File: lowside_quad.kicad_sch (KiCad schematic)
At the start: 18 parts, among them U30 RED, U31 RED, U32 RED, U33 RED, U39 1N4148WS, U40 1N4148WS, U45 1N4148WS, U46 1N4148WS, U47 VND7NV04TR-E, U48 VND7NV04TR-E, U49 VND7NV04TR-E, U50 VND7NV04TR-E

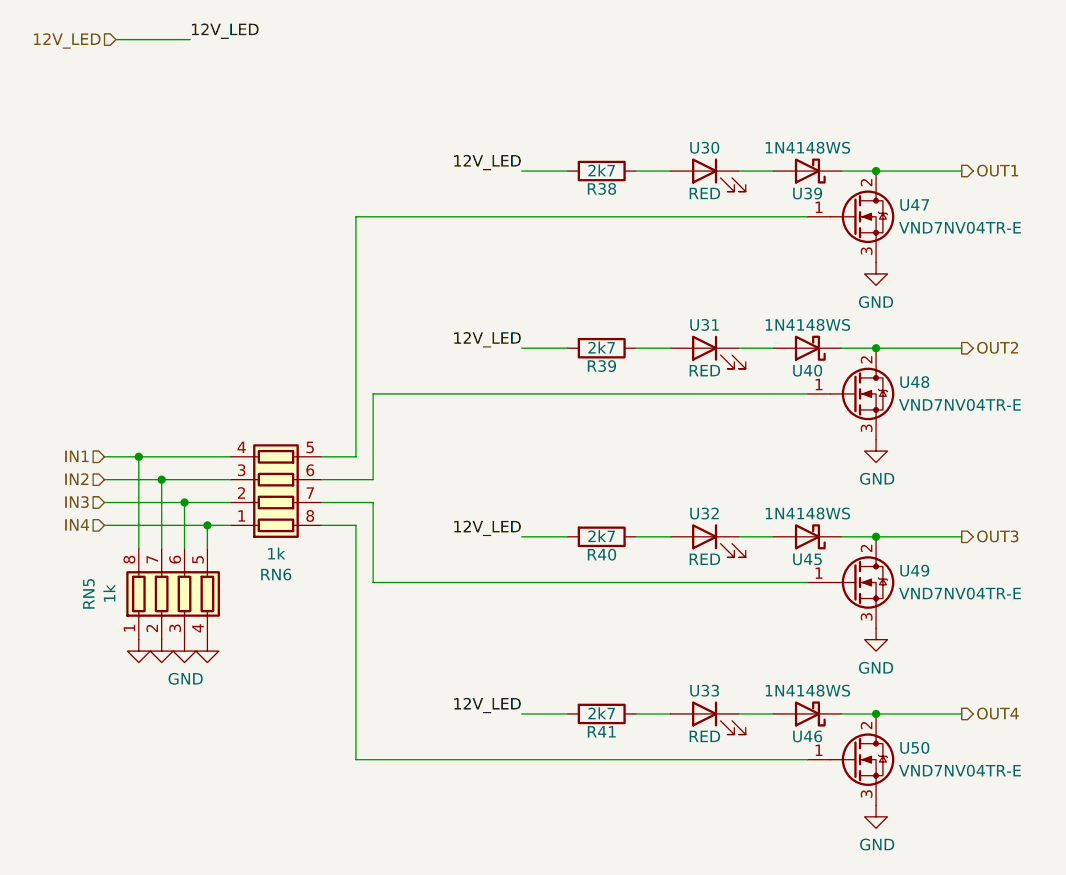
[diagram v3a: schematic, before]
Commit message: Production optimizations, voltage superv, etb sv conn
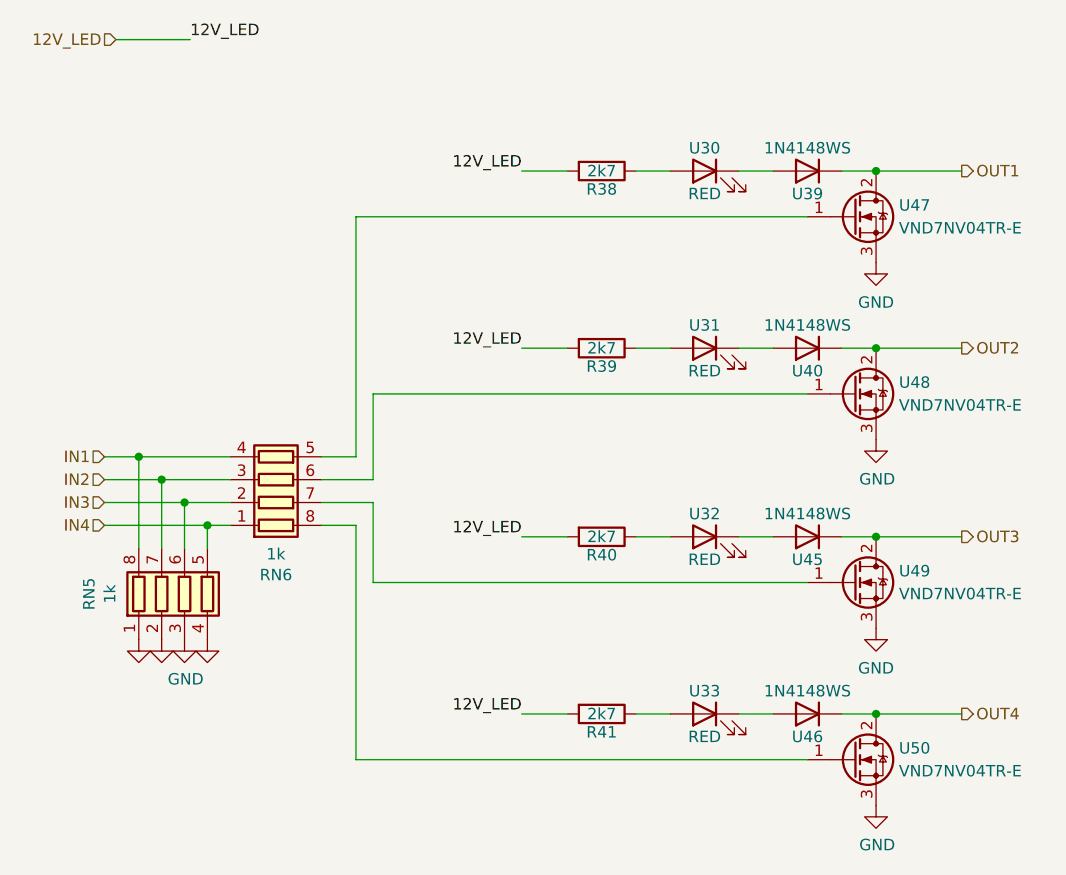
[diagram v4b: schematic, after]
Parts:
- U39, U40, U45, U46: symbol Device:D_Schottky -> Device:D
- U47, U48, U49, U50: footprint Package_TO_SOT_SMD:TO-252-2 -> Package_TO_SOT_SMD:TO-252-3_TabPin2; JLCPosOffset (none) -> 2,0; JLCRotOffset (none) -> 180; LCSC C155605 -> C262999; LCSC_alt (none) -> C155605
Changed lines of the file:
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@@
       (effects (font (size 1.27 1.27)) (justify left))
     )
-    (property "Footprint" "Package_TO_SOT_SMD:TO-252-2" (at 147.32 99.695 0)
+    (property "Footprint" "Package_TO_SOT_SMD:TO-252-3_TabPin2" (at 147.32 99.695 0)
       (effects (font (size 1.27 1.27)) hide)
     )
@@
       (effects (font (size 1.27 1.27)) hide)
     )
-    (property "LCSC" "C155605" (at 142.24 102.235 0)
+    (property "LCSC" "C262999" (at 142.24 102.235 0)
+      (effects (font (size 1.27 1.27)) hide)
+    )
+    (property "JLCPosOffset" "2,0" (at 142.24 102.235 0)
+      (effects (font (size 1.27 1.27)) hide)
+    )
+    (property "LCSC_alt" "C155605" (at 142.24 102.235 0)
+      (effects (font (size 1.27 1.27)) hide)
+    )
+    (property "JLCRotOffset" "180" (at 142.24 102.235 0)
       (effects (font (size 1.27 1.27)) hide)
     )
@@
     )
   )
-  (symbol (lib_id "Device:D_Schottky") (at 137.16 36.83 180) (unit 1)
+  (symbol (lib_id "Device:D") (at 137.16 36.83 180) (unit 1)
     (in_bom yes) (on_board yes) (dnp no)
     (property "Reference" "U39" (at 137.16 39.37 0)
@@
       (effects (font (size 1.27 1.27)) hide)
     )
-    (property "Datasheet" "" (at 137.16 36.83 0)
-      (effects (font (size 1.27 1.27)))
+    (property "Datasheet" "~" (at 137.16 36.83 0)
+      (effects (font (size 1.27 1.27)) hide)
     )
     (property "LCSC" "C2128" (at 137.16 36.83 0)
       (effects (font (size 1.27 1.27)) hide)
     )
+    (property "Sim.Device" "D" (at 137.16 36.83 0)
+      (effects (font (size 1.27 1.27)) hide)
+    )
+    (property "Sim.Pins" "1=K 2=A" (at 137.16 36.83 0)
+      (effects (font (size 1.27 1.27)) hide)
+    )
     (pin "1")
     (pin "2")
@@
       (effects (font (size 1.27 1.27)) (justify left))
     )
-    (property "Footprint" "Package_TO_SOT_SMD:TO-252-2" (at 147.32 39.37 0)
+    (property "Footprint" "Package_TO_SOT_SMD:TO-252-3_TabPin2" (at 147.32 39.37 0)
       (effects (font (size 1.27 1.27)) hide)
     )
@@
       (effects (font (size 1.27 1.27)) hide)
     )
-    (property "LCSC" "C155605" (at 142.24 41.91 0)
+    (property "LCSC" "C262999" (at 142.24 41.91 0)
+      (effects (font (size 1.27 1.27)) hide)
+    )
+    (property "JLCPosOffset" "2,0" (at 142.24 41.91 0)
+      (effects (font (size 1.27 1.27)) hide)
+    )
+    (property "LCSC_alt" "C155605" (at 142.24 41.91 0)
+      (effects (font (size 1.27 1.27)) hide)
+    )
+    (property "JLCRotOffset" "180" (at 142.24 41.91 0)
       (effects (font (size 1.27 1.27)) hide)
     )
@@
     )
   )
-  (symbol (lib_id "Device:D_Schottky") (at 137.16 97.155 180) (unit 1)
+  (symbol (lib_id "Device:D") (at 137.16 97.155 180) (unit 1)
     (in_bom yes) (on_board yes) (dnp no)
     (property "Reference" "U46" (at 137.16 99.695 0)
@@
       (effects (font (size 1.27 1.27)) hide)
     )
-    (property "Datasheet" "" (at 137.16 97.155 0)
-      (effects (font (size 1.27 1.27)))
+    (property "Datasheet" "~" (at 137.16 97.155 0)
+      (effects (font (size 1.27 1.27)) hide)
     )
     (property "LCSC" "C2128" (at 137.16 97.155 0)
       (effects (font (size 1.27 1.27)) hide)
     )
+    (property "Sim.Device" "D" (at 137.16 97.155 0)
+      (effects (font (size 1.27 1.27)) hide)
+    )
+    (property "Sim.Pins" "1=K 2=A" (at 137.16 97.155 0)
+      (effects (font (size 1.27 1.27)) hide)
+    )
     (pin "1")
     (pin "2")
@@
       (effects (font (size 1.27 1.27)) (justify left))
     )
-    (property "Footprint" "Package_TO_SOT_SMD:TO-252-2" (at 147.32 80.01 0)
+    (property "Footprint" "Package_TO_SOT_SMD:TO-252-3_TabPin2" (at 147.32 80.01 0)
       (effects (font (size 1.27 1.27)) hide)
     )
@@
       (effects (font (size 1.27 1.27)) hide)
     )
-    (property "LCSC" "C155605" (at 142.24 82.55 0)
+    (property "LCSC" "C262999" (at 142.24 82.55 0)
+      (effects (font (size 1.27 1.27)) hide)
+    )
+    (property "JLCPosOffset" "2,0" (at 142.24 82.55 0)
+      (effects (font (size 1.27 1.27)) hide)
+    )
+    (property "LCSC_alt" "C155605" (at 142.24 82.55 0)
+      (effects (font (size 1.27 1.27)) hide)
+    )
+    (property "JLCRotOffset" "180" (at 142.24 82.55 0)
       (effects (font (size 1.27 1.27)) hide)
     )
@@
     )
   )
-  (symbol (lib_id "Device:D_Schottky") (at 137.16 56.515 180) (unit 1)
+  (symbol (lib_id "Device:D") (at 137.16 56.515 180) (unit 1)
     (in_bom yes) (on_board yes) (dnp no)
     (property "Reference" "U40" (at 137.16 59.055 0)
@@
       (effects (font (size 1.27 1.27)) hide)
     )
-    (property "Datasheet" "" (at 137.16 56.515 0)
-      (effects (font (size 1.27 1.27)))
+    (property "Datasheet" "~" (at 137.16 56.515 0)
+      (effects (font (size 1.27 1.27)) hide)
     )
     (property "LCSC" "C2128" (at 137.16 56.515 0)
       (effects (font (size 1.27 1.27)) hide)
     )
+    (property "Sim.Device" "D" (at 137.16 56.515 0)
+      (effects (font (size 1.27 1.27)) hide)
+    )
+    (property "Sim.Pins" "1=K 2=A" (at 137.16 56.515 0)
+      (effects (font (size 1.27 1.27)) hide)
+    )
     (pin "1")
     (pin "2")
@@
       (effects (font (size 1.27 1.27)) (justify left))
     )
-    (property "Footprint" "Package_TO_SOT_SMD:TO-252-2" (at 147.32 59.055 0)
+    (property "Footprint" "Package_TO_SOT_SMD:TO-252-3_TabPin2" (at 147.32 59.055 0)
       (effects (font (size 1.27 1.27)) hide)
     )
@@
       (effects (font (size 1.27 1.27)) hide)
     )
-    (property "LCSC" "C155605" (at 142.24 61.595 0)
+    (property "LCSC" "C262999" (at 142.24 61.595 0)
+      (effects (font (size 1.27 1.27)) hide)
+    )
+    (property "JLCPosOffset" "2,0" (at 142.24 61.595 0)
+      (effects (font (size 1.27 1.27)) hide)
+    )
+    (property "LCSC_alt" "C155605" (at 142.24 61.595 0)
+      (effects (font (size 1.27 1.27)) hide)
+    )
+    (property "JLCRotOffset" "180" (at 142.24 61.595 0)
       (effects (font (size 1.27 1.27)) hide)
     )
@@
     )
   )
-  (symbol (lib_id "Device:D_Schottky") (at 137.16 77.47 180) (unit 1)
+  (symbol (lib_id "Device:D") (at 137.16 77.47 180) (unit 1)
     (in_bom yes) (on_board yes) (dnp no)
     (property "Reference" "U45" (at 137.16 80.01 0)
@@
       (effects (font (size 1.27 1.27)) hide)
     )
-    (property "Datasheet" "" (at 137.16 77.47 0)
-      (effects (font (size 1.27 1.27)))
+    (property "Datasheet" "~" (at 137.16 77.47 0)
+      (effects (font (size 1.27 1.27)) hide)
     )
     (property "LCSC" "C2128" (at 137.16 77.47 0)
       (effects (font (size 1.27 1.27)) hide)
     )
+    (property "Sim.Device" "D" (at 137.16 77.47 0)
+      (effects (font (size 1.27 1.27)) hide)
+    )
+    (property "Sim.Pins" "1=K 2=A" (at 137.16 77.47 0)
+      (effects (font (size 1.27 1.27)) hide)
+    )
